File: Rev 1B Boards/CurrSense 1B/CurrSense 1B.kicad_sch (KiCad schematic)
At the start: 19 parts, among them J1 Conn_01x01_Pin, J10 Conn_01x01_Pin, J13 Banana 2P, J14 Banana 2P, J15 Banana 2P, J2 Conn_01x01_Pin, J3 XT30_F, J4 Banana 2P, J5 Banana 2P, J6 XT30_F, J7 XT30_F, J8 Banana 2P, J9 XT30_F, Q1 BSC059N04LS6, Q2 BSC059N04LS6

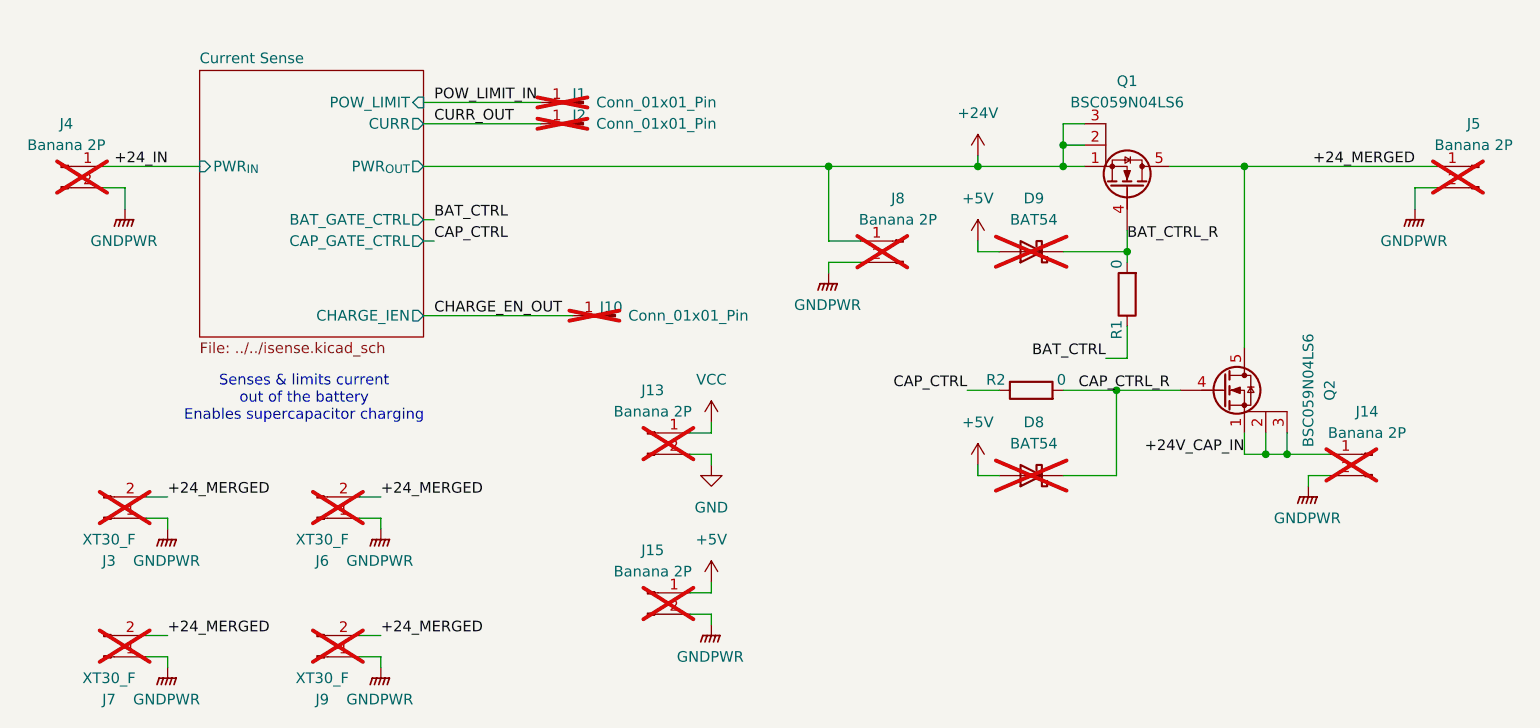
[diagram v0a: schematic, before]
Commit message: Add labels + more test points
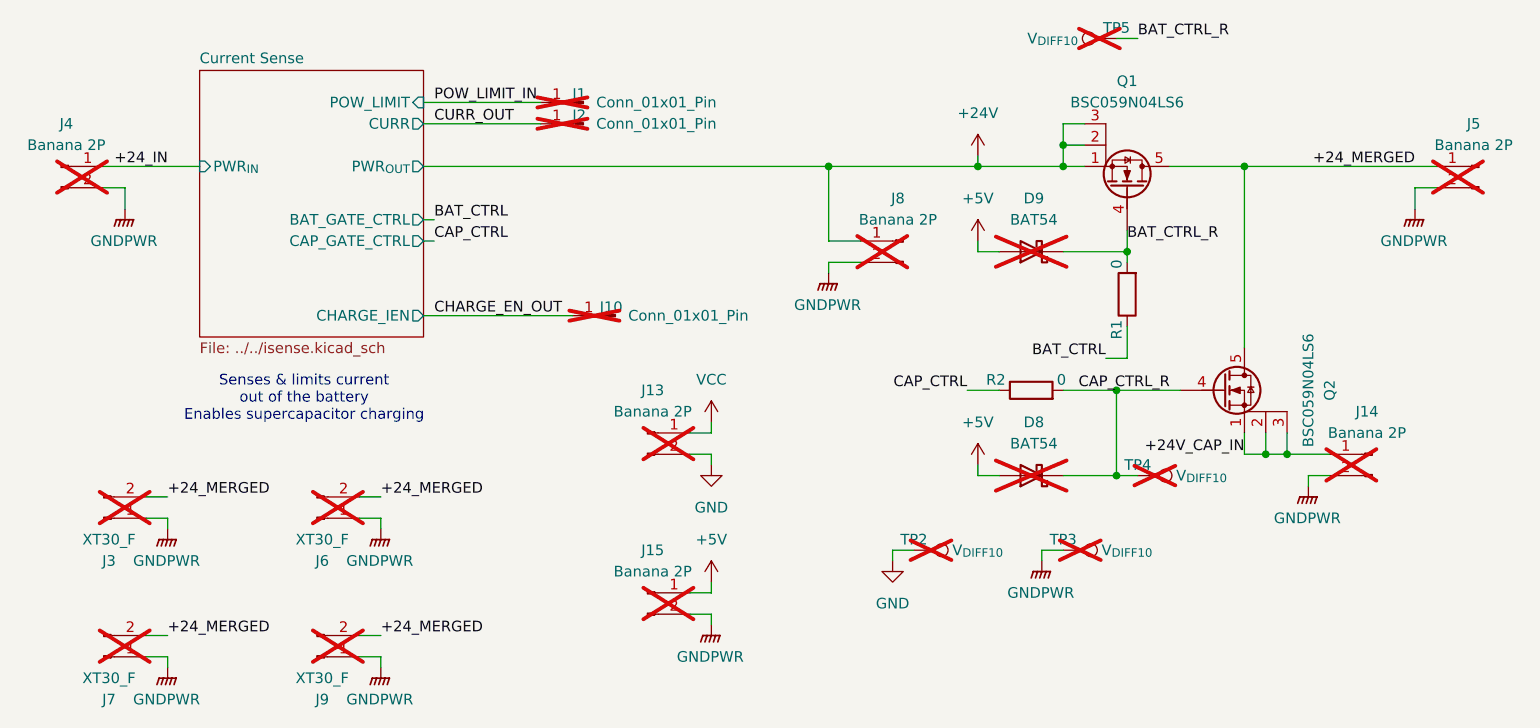
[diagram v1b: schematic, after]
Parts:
- added TP2, TP3: V_{DIFF10}, TestPoint:TestPoint_Bridge_Pitch2.0mm_Drill0.7mm, symbol Connector:TestPoint
- added TP4, TP5: V_{DIFF10}, TestPoint:TestPoint_Pad_1.0x1.0mm, symbol Connector:TestPoint
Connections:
- net BAT_CTRL_R: now also TP5.1
- net CAP_CTRL_R: now also TP4.1
- net GND: now also TP2.1
- net GNDPWR: now also TP3.1

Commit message: Replace most banana jacks with XT connectors
+ update library
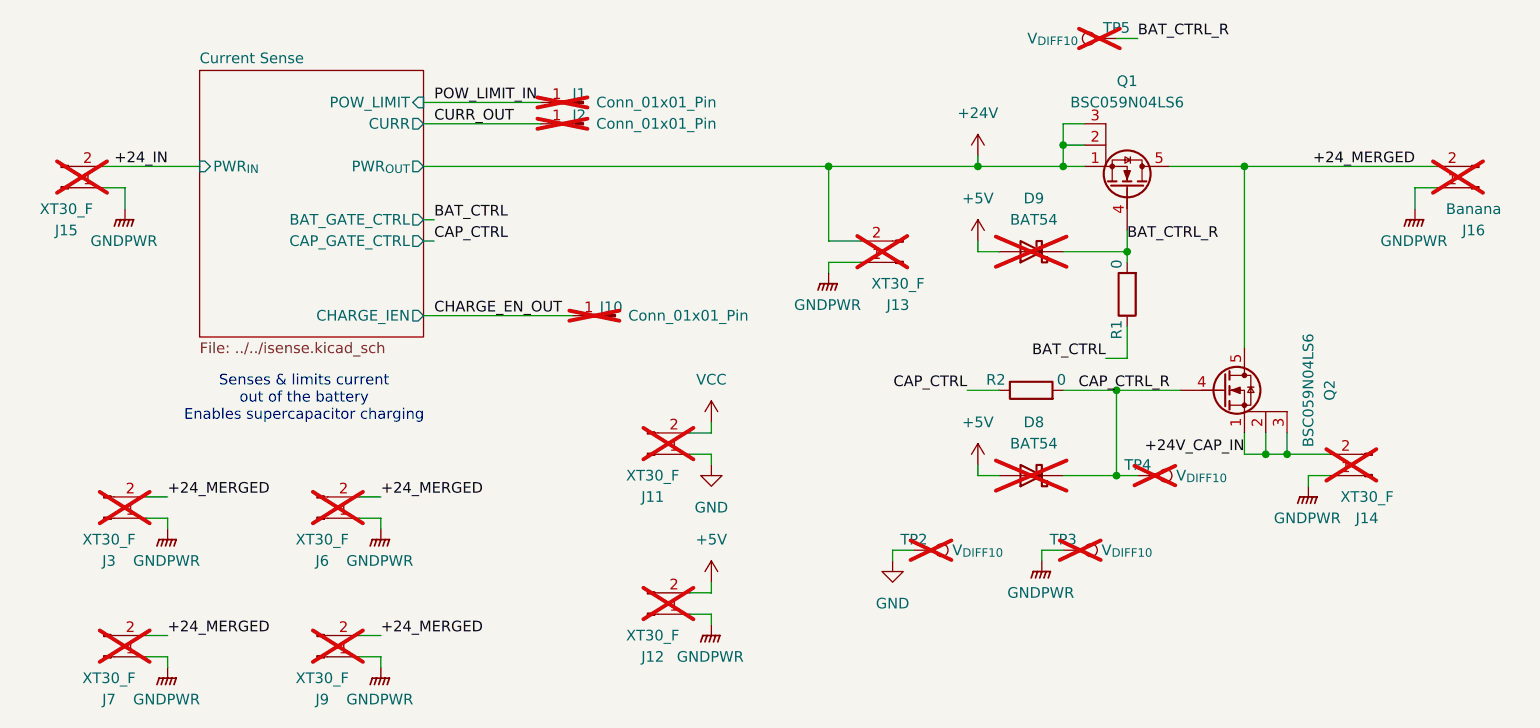
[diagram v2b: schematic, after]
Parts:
- removed J4, J5, J8: Banana 2P, Connector:Banana_Jack_2Pin, symbol Connector:Conn_01x02_Pin
- added J11, J12: XT30_F, Connector_AMASS:AMASS_XT30U-F_1x02_P5.0mm_Vertical, symbol Connector:Conn_01x02_Pin
- added J16: Banana, ! Robomaster Connectors:RM_Banana_Jack_2Pin, symbol Connector:Conn_01x02_Pin
- J13, J14, J15: value Banana 2P -> XT30_F; footprint Connector:Banana_Jack_2Pin -> Connector_AMASS:AMASS_XT30U-F_1x02_P5.0mm_Vertical
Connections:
- net +24V: now also J13.2 (Pin_2)
- net +24V_CAP_IN: now also J14.2 (Pin_2); no longer J14.1 (Pin_1)
- net +24_IN: now also J15.2 (Pin_2)
- net +24_MERGED: now also J16.2 (Pin_2)
- net +5V: now also J12.2 (Pin_2); no longer J15.1 (Pin_1)
- net GND: now also J11.1 (Pin_1); no longer J13.2 (Pin_2)
- net GNDPWR: now also J13.1 (Pin_1), J14.1 (Pin_1), J15.1 (Pin_1), J12.1 (Pin_1), J16.1 (Pin_1); no longer J14.2 (Pin_2), J15.2 (Pin_2)
- net VCC: now also J11.2 (Pin_2); no longer J13.1 (Pin_1)

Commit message: added test points to current sense PCB
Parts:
- TP4, TP5: footprint TestPoint:TestPoint_Pad_1.0x1.0mm -> TestPoint:TestPoint_Bridge_Pitch2.0mm_Drill0.7mm
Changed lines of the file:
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@@
 			)
 		)
-		(property "Footprint" "TestPoint:TestPoint_Pad_1.0x1.0mm"
+		(property "Footprint" "TestPoint:TestPoint_Bridge_Pitch2.0mm_Drill0.7mm"
 			(at 148.59 74.93 0)
 			(effects
@@
 			)
 		)
-		(property "Footprint" "TestPoint:TestPoint_Pad_1.0x1.0mm"
+		(property "Footprint" "TestPoint:TestPoint_Bridge_Pitch2.0mm_Drill0.7mm"
 			(at 146.05 22.86 0)
 			(effects
